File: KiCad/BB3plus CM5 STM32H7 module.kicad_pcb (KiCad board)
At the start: 6 copper layers, 55 x 40 mm, 163 parts, among them IC1 AZ1117CH2-3.3TRG1, IC10 LSF0204GU12, IC11 MX25UM25645GXDI00-T, IC2 AZ1117CH-1.8TRG1, IC3 PI3USB102ZLEX, IC4 SN74LVC1G14DBVR, IC5 STM32H7R7L8H6H, IC6 LAN8742A-CZ-TR, IC7 APS256XXN-OBR-BG, IC8 TFP410PAP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

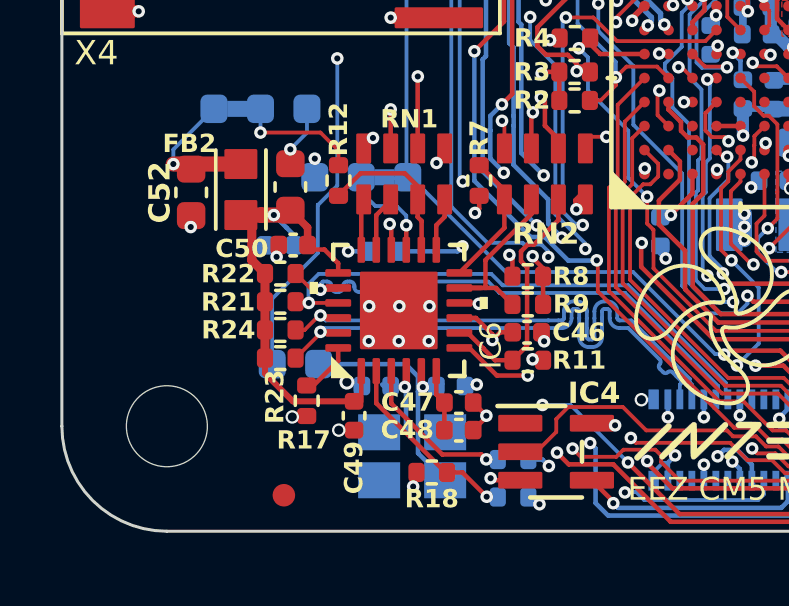
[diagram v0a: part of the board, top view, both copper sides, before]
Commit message: Ethernet PHY no xtal variant added
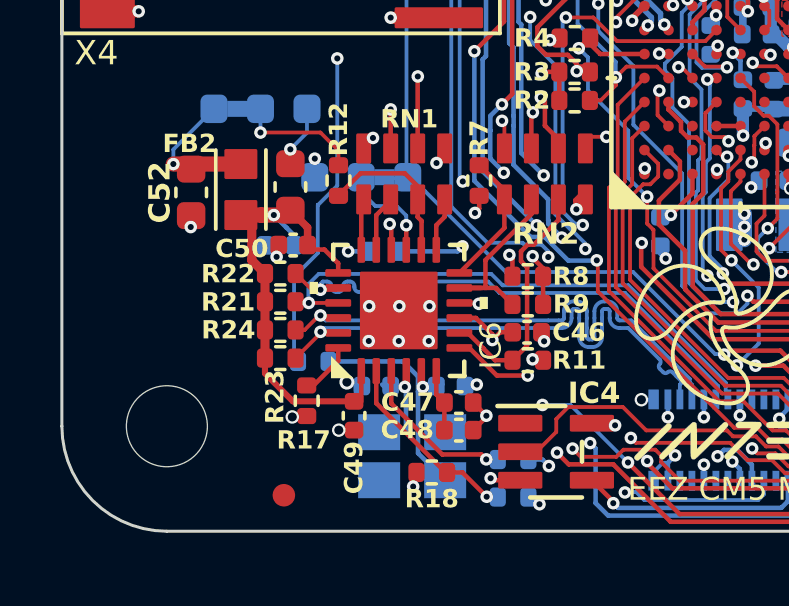
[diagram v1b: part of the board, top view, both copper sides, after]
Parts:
- JP3: footprint PCM_EEZ_SMD:JP2 open (0603) -> PCM_EEZ_SMD:JP2 open (0402)
- moved JP3 0.61 mm to (102.5, 106.5)

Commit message: #23
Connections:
- IC5 pad L13: unconnected-(IC5A-PD15-PadL13) -> GND
- IC5 pad N13: unconnected-(IC5A-PD12-PadN13) -> GND
- IC5 pad P14: unconnected-(IC5A-PD13-PadP14) -> GND
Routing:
- net GND: track 108.2 -> 110.8 mm, vias 254 -> 256
